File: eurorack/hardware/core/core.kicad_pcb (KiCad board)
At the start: 4 copper layers, 19.3 x 69.8 mm, 51 parts, among them J1 ConnNW, J2 ConnSW, J3 ConnNE, J4 ConnSE, J5 Power, J6 SWD, SW1 Reset, SW2 Boot0, U1 STM32F427VGT6, U2 TLV320AIC23BPW, U3 LM1117F-3.3, U4 LM4040C10IDBZR, Y1 Crystal

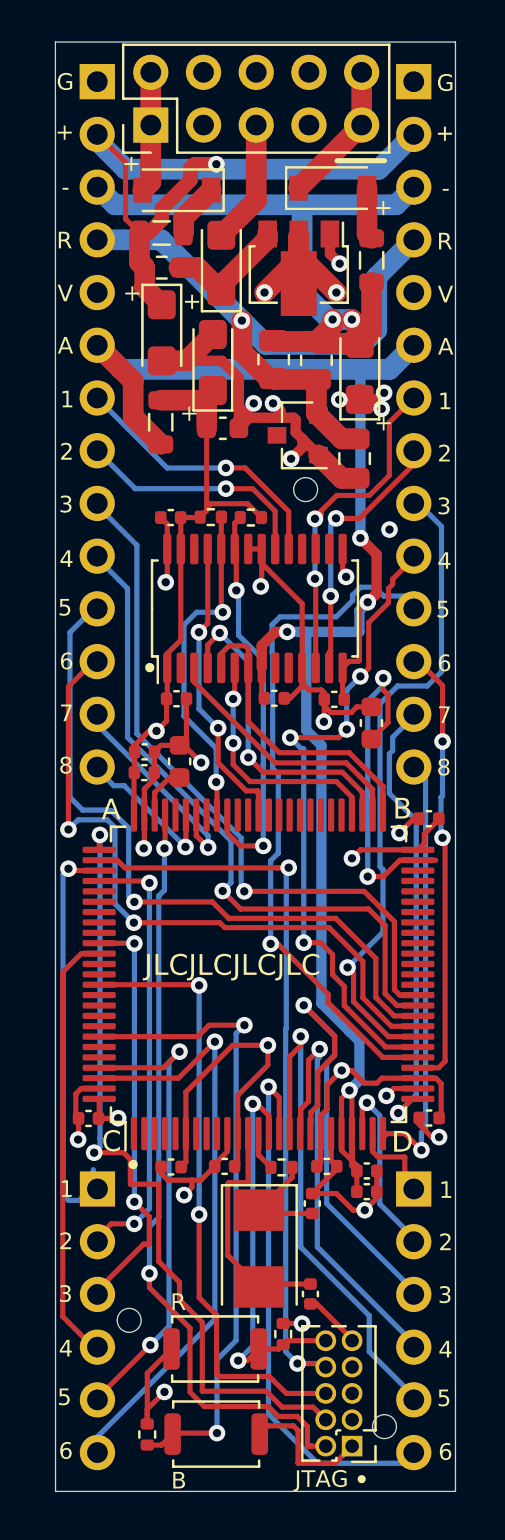
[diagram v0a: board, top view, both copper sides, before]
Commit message: Increase the height to 20 mm
Signed-off-by: Petr Horacek <hrck@protonmail.com>
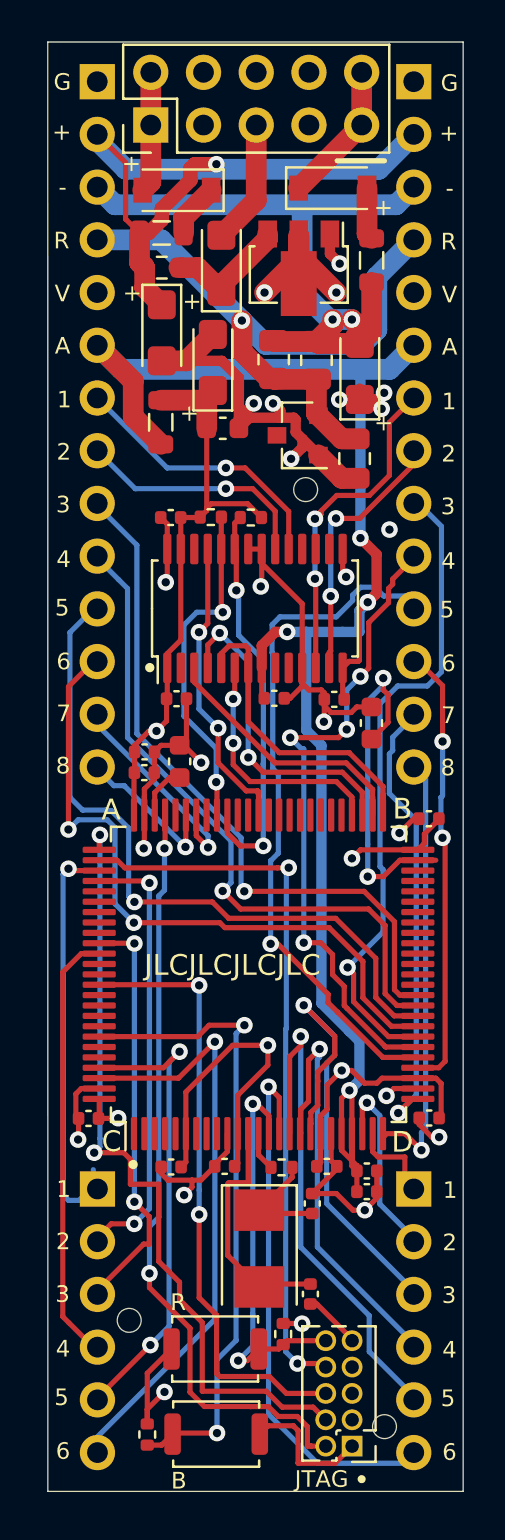
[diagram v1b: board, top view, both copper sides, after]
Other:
- board size 19.3 x 69.8 mm -> 20 x 69.8 mm
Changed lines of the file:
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@@
       (usegerberattributes true)
       (usegerberadvancedattributes true)
-      (creategerberjobfile true)
+      (creategerberjobfile false)
       (excludeedgelayer true)
       (linewidth 0.100000)
@@
   )
   (gr_line (start 154.314 70.75) (end 156.6 70.75) (layer F.SilkS) (width 0.25))
-  (gr_line (start 160.02 65.03) (end 140.75 65.03) (layer Edge.Cuts) (width 0.05))
-  (gr_line (start 160.02 134.86) (end 160.02 65.03) (layer Edge.Cuts) (width 0.05))
+  (gr_line (start 160.39 65.03) (end 140.375 65.03) (layer Edge.Cuts) (width 0.05))
+  (gr_line (start 160.39 134.86) (end 160.39 65.03) (layer Edge.Cuts) (width 0.05))
   (gr_circle (center 144.49 119.11) (end 144.604018 119.11) (layer F.SilkS) (width 0.22))
   (gr_circle (center 145.29 95.17) (end 145.404018 95.17) (layer F.SilkS) (width 0.22))
-  (gr_text - (at 159.55 72.08) (layer F.SilkS)
-    (effects (font (size 0.8 0.8) (thickness 0.15)))
-  )
-  (gr_text V (at 159.54 77.2) (layer F.SilkS)
-    (effects (font (size 0.8 0.8) (thickness 0.15)))
-  )
-  (gr_text + (at 159.51 69.42) (layer F.SilkS)
-    (effects (font (size 0.8 0.8) (thickness 0.15)))
-  )
-  (gr_text R (at 159.5 74.65) (layer F.SilkS)
-    (effects (font (size 0.8 0.8) (thickness 0.15)))
-  )
-  (gr_text G (at 159.54 67.01) (layer F.SilkS)
-    (effects (font (size 0.8 0.8) (thickness 0.15)))
-  )
-  (gr_text A (at 159.55 79.72) (layer F.SilkS)
-    (effects (font (size 0.8 0.8) (thickness 0.15)))
-  )
-  (gr_text 2 (at 141.26 122.82) (layer F.SilkS)
-    (effects (font (size 0.8 0.8) (thickness 0.15)))
-  )
-  (gr_text 1 (at 141.28 120.3) (layer F.SilkS)
-    (effects (font (size 0.8 0.8) (thickness 0.15)))
-  )
-  (gr_text 6 (at 141.25 132.92) (layer F.SilkS)
-    (effects (font (size 0.8 0.8) (thickness 0.15)))
-  )
-  (gr_text 3 (at 141.23 125.36) (layer F.SilkS)
-    (effects (font (size 0.8 0.8) (thickness 0.15)))
-  )
-  (gr_text 4 (at 141.25 127.99) (layer F.SilkS)
-    (effects (font (size 0.8 0.8) (thickness 0.15)))
-  )
-  (gr_text 5 (at 141.18 130.33) (layer F.SilkS)
-    (effects (font (size 0.8 0.8) (thickness 0.15)))
-  )
-  (gr_text 2 (at 159.55 122.87) (layer F.SilkS)
-    (effects (font (size 0.8 0.8) (thickness 0.15)))
-  )
-  (gr_text 1 (at 159.57 120.35) (layer F.SilkS)
-    (effects (font (size 0.8 0.8) (thickness 0.15)))
-  )
-  (gr_text 6 (at 159.54 132.97) (layer F.SilkS)
-    (effects (font (size 0.8 0.8) (thickness 0.15)))
-  )
-  (gr_text 3 (at 159.52 125.41) (layer F.SilkS)
-    (effects (font (size 0.8 0.8) (thickness 0.15)))
-  )
-  (gr_text 4 (at 159.54 128.04) (layer F.SilkS)
-    (effects (font (size 0.8 0.8) (thickness 0.15)))
-  )
-  (gr_text 5 (at 159.47 130.38) (layer F.SilkS)
-    (effects (font (size 0.8 0.8) (thickness 0.15)))
-  )
-  (gr_text 2 (at 159.5 84.87) (layer F.SilkS)
-    (effects (font (size 0.8 0.8) (thickness 0.15)))
-  )
-  (gr_text 1 (at 159.52 82.35) (layer F.SilkS)
-    (effects (font (size 0.8 0.8) (thickness 0.15)))
-  )
-  (gr_text 6 (at 159.49 94.97) (layer F.SilkS)
-    (effects (font (size 0.8 0.8) (thickness 0.15)))
-  )
-  (gr_text 3 (at 159.47 87.41) (layer F.SilkS)
-    (effects (font (size 0.8 0.8) (thickness 0.15)))
-  )
-  (gr_text 4 (at 159.49 90.04) (layer F.SilkS)
-    (effects (font (size 0.8 0.8) (thickness 0.15)))
-  )
-  (gr_text 5 (at 159.42 92.38) (layer F.SilkS)
-    (effects (font (size 0.8 0.8) (thickness 0.15)))
-  )
-  (gr_text 8 (at 159.46 99.99) (layer F.SilkS)
-    (effects (font (size 0.8 0.8) (thickness 0.15)))
-  )
-  (gr_text 7 (at 159.49 97.47) (layer F.SilkS)
+  (gr_text - (at 159.74 72.08) (layer F.SilkS)
+    (effects (font (size 0.8 0.8) (thickness 0.15)))
+  )
+  (gr_text V (at 159.73 77.2) (layer F.SilkS)
+    (effects (font (size 0.8 0.8) (thickness 0.15)))
+  )
+  (gr_text + (at 159.7 69.42) (layer F.SilkS)
+    (effects (font (size 0.8 0.8) (thickness 0.15)))
+  )
+  (gr_text R (at 159.69 74.65) (layer F.SilkS)
+    (effects (font (size 0.8 0.8) (thickness 0.15)))
+  )
+  (gr_text G (at 159.73 67.01) (layer F.SilkS)
+    (effects (font (size 0.8 0.8) (thickness 0.15)))
+  )
+  (gr_text A (at 159.74 79.72) (layer F.SilkS)
+    (effects (font (size 0.8 0.8) (thickness 0.15)))
+  )
+  (gr_text 2 (at 141.12 122.82) (layer F.SilkS)
+    (effects (font (size 0.8 0.8) (thickness 0.15)))
+  )
+  (gr_text 1 (at 141.14 120.3) (layer F.SilkS)
+    (effects (font (size 0.8 0.8) (thickness 0.15)))
+  )
+  (gr_text 6 (at 141.11 132.92) (layer F.SilkS)
+    (effects (font (size 0.8 0.8) (thickness 0.15)))
+  )
+  (gr_text 3 (at 141.09 125.36) (layer F.SilkS)
+    (effects (font (size 0.8 0.8) (thickness 0.15)))
+  )
+  (gr_text 4 (at 141.11 127.99) (layer F.SilkS)
+    (effects (font (size 0.8 0.8) (thickness 0.15)))
+  )
+  (gr_text 5 (at 141.04 130.33) (layer F.SilkS)
+    (effects (font (size 0.8 0.8) (thickness 0.15)))
+  )
+  (gr_text 2 (at 159.74 122.87) (layer F.SilkS)
+    (effects (font (size 0.8 0.8) (thickness 0.15)))
+  )
+  (gr_text 1 (at 159.76 120.35) (layer F.SilkS)
+    (effects (font (size 0.8 0.8) (thickness 0.15)))
+  )
+  (gr_text 6 (at 159.73 132.97) (layer F.SilkS)
+    (effects (font (size 0.8 0.8) (thickness 0.15)))
+  )
+  (gr_text 3 (at 159.71 125.41) (layer F.SilkS)
+    (effects (font (size 0.8 0.8) (thickness 0.15)))
+  )
+  (gr_text 4 (at 159.73 128.04) (layer F.SilkS)
+    (effects (font (size 0.8 0.8) (thickness 0.15)))
+  )
+  (gr_text 5 (at 159.66 130.38) (layer F.SilkS)
+    (effects (font (size 0.8 0.8) (thickness 0.15)))
+  )
+  (gr_text 2 (at 159.69 84.87) (layer F.SilkS)
+    (effects (font (size 0.8 0.8) (thickness 0.15)))
+  )
+  (gr_text 1 (at 159.71 82.35) (layer F.SilkS)
+    (effects (font (size 0.8 0.8) (thickness 0.15)))
+  )
+  (gr_text 6 (at 159.68 94.97) (layer F.SilkS)
+    (effects (font (size 0.8 0.8) (thickness 0.15)))
+  )
+  (gr_text 3 (at 159.66 87.41) (layer F.SilkS)
+    (effects (font (size 0.8 0.8) (thickness 0.15)))
+  )
+  (gr_text 4 (at 159.68 90.04) (layer F.SilkS)
+    (effects (font (size 0.8 0.8) (thickness 0.15)))
+  )
+  (gr_text 5 (at 159.61 92.38) (layer F.SilkS)
+    (effects (font (size 0.8 0.8) (thickness 0.15)))
+  )
+  (gr_text 8 (at 159.65 99.99) (layer F.SilkS)
+    (effects (font (size 0.8 0.8) (thickness 0.15)))
+  )
+  (gr_text 7 (at 159.68 97.47) (layer F.SilkS)
     (effects (font (size 0.8 0.8) (thickness 0.15)))
   )
@@
     (effects (font (size 1 1) (thickness 0.15)))
   )
-  (gr_text 8 (at 141.25 99.9) (layer F.SilkS)
-    (effects (font (size 0.8 0.8) (thickness 0.15)))
-  )
-  (gr_text 7 (at 141.28 97.38) (layer F.SilkS)
-    (effects (font (size 0.8 0.8) (thickness 0.15)))
-  )
-  (gr_text 6 (at 141.28 94.88) (layer F.SilkS)
-    (effects (font (size 0.8 0.8) (thickness 0.15)))
-  )
-  (gr_text 5 (at 141.21 92.29) (layer F.SilkS)
-    (effects (font (size 0.8 0.8) (thickness 0.15)))
-  )
-  (gr_text 4 (at 141.28 89.95) (layer F.SilkS)
-    (effects (font (size 0.8 0.8) (thickness 0.15)))
-  )
-  (gr_text 3 (at 141.26 87.32) (layer F.SilkS)
-    (effects (font (size 0.8 0.8) (thickness 0.15)))
-  )
-  (gr_text 1 (at 141.31 82.26) (layer F.SilkS)
-    (effects (font (size 0.8 0.8) (thickness 0.15)))
-  )
-  (gr_text 2 (at 141.29 84.78) (layer F.SilkS)
-    (effects (font (size 0.8 0.8) (thickness 0.15)))
-  )
-  (gr_text A (at 141.23 79.67) (layer F.SilkS)
-    (effects (font (size 0.8 0.8) (thickness 0.15)))
-  )
-  (gr_text V (at 141.22 77.15) (layer F.SilkS)
-    (effects (font (size 0.8 0.8) (thickness 0.15)))
-  )
-  (gr_text - (at 141.23 72.03) (layer F.SilkS)
-    (effects (font (size 0.8 0.8) (thickness 0.15)))
-  )
-  (gr_text R (at 141.18 74.6) (layer F.SilkS)
-    (effects (font (size 0.8 0.8) (thickness 0.15)))
-  )
-  (gr_text + (at 141.19 69.37) (layer F.SilkS)
-    (effects (font (size 0.8 0.8) (thickness 0.15)))
-  )
-  (gr_text G (at 141.22 66.96) (layer F.SilkS)
+  (gr_text 8 (at 141.11 99.9) (layer F.SilkS)
+    (effects (font (size 0.8 0.8) (thickness 0.15)))
+  )
+  (gr_text 7 (at 141.14 97.38) (layer F.SilkS)
+    (effects (font (size 0.8 0.8) (thickness 0.15)))
+  )
+  (gr_text 6 (at 141.14 94.88) (layer F.SilkS)
+    (effects (font (size 0.8 0.8) (thickness 0.15)))
+  )
+  (gr_text 5 (at 141.07 92.29) (layer F.SilkS)
+    (effects (font (size 0.8 0.8) (thickness 0.15)))
+  )
+  (gr_text 4 (at 141.14 89.95) (layer F.SilkS)
+    (effects (font (size 0.8 0.8) (thickness 0.15)))
+  )
+  (gr_text 3 (at 141.12 87.32) (layer F.SilkS)
+    (effects (font (size 0.8 0.8) (thickness 0.15)))
+  )
+  (gr_text 1 (at 141.17 82.26) (layer F.SilkS)
+    (effects (font (size 0.8 0.8) (thickness 0.15)))
+  )
+  (gr_text 2 (at 141.15 84.78) (layer F.SilkS)
+    (effects (font (size 0.8 0.8) (thickness 0.15)))
+  )
+  (gr_text A (at 141.09 79.67) (layer F.SilkS)
+    (effects (font (size 0.8 0.8) (thickness 0.15)))
+  )
+  (gr_text V (at 141.08 77.15) (layer F.SilkS)
+    (effects (font (size 0.8 0.8) (thickness 0.15)))
+  )
+  (gr_text - (at 141.09 72.03) (layer F.SilkS)
+    (effects (font (size 0.8 0.8) (thickness 0.15)))
+  )
+  (gr_text R (at 141.04 74.6) (layer F.SilkS)
+    (effects (font (size 0.8 0.8) (thickness 0.15)))
+  )
+  (gr_text + (at 141.05 69.37) (layer F.SilkS)
+    (effects (font (size 0.8 0.8) (thickness 0.15)))
+  )
+  (gr_text G (at 141.08 66.96) (layer F.SilkS)
     (effects (font (size 0.8 0.8) (thickness 0.15)))
   )
@@
     (effects (font (size 0.8 0.8) (thickness 0.15)))
   )
-  (gr_line (start 140.745 65.03) (end 140.75 134.86) (layer Edge.Cuts) (width 0.05))
-  (gr_line (start 140.75 134.86) (end 160.02 134.86) (layer Edge.Cuts) (width 0.05))
+  (gr_line (start 140.375 65.03) (end 140.38 134.86) (layer Edge.Cuts) (width 0.05))
+  (gr_line (start 140.38 134.86) (end 160.39 134.86) (layer Edge.Cuts) (width 0.05))
   (segment (start 152.15 119.730002) (end 150.570001 121.310001) (width 0.25) (layer F.Cu) (net 54) (status 20))
   (segment (start 152.15 119.25) (end 152.15 119.730002) (width 0.25) (layer F.Cu) (net 54) (status 10))

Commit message: Switch to STM32H743VIT6
It is twice the price of STM32F4 on JLCPCB and twice as fast.

Signed-off-by: Petr Horacek <hrck@protonmail.com>
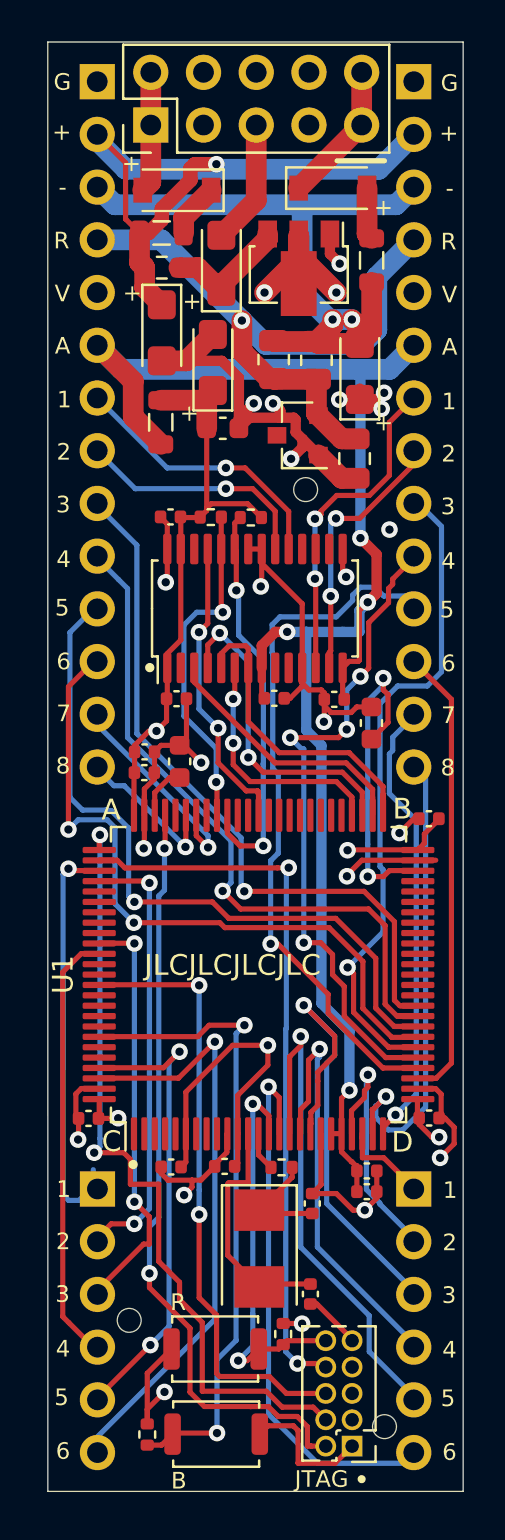
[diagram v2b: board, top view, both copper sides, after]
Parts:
- removed C19: 100n, Capacitor_SMD:C_0402_1005Metric
- U1: value STM32F427VGT6 -> STM32H743VIT6
- moved C15 32.2 mm to (146.3, 87.9), turned to 180 degrees
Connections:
- U1 pad 19: +3V3 -> GND
- U1 pad 20: GND -> +3.3VA
- U1 pad 22: +3.3VA -> PIN20
- U1 pad 23: PIN20 -> PIN19
- U1 pad 24: PIN19 -> PIN18
- U1 pad 25: PIN18 -> PIN17
- U1 pad 26: PIN17 -> GND
- U1 pad 27: GND -> +3V3
- U1 pad 28: +3V3 -> PIN16
- U1 pad 29: PIN16 -> PIN15
- U1 pad 30: PIN15 -> PIN14
- U1 pad 31: PIN14 -> PIN13
- U1 pad 32: PIN13 -> PIN4
- U1 pad 33: PIN4 -> PIN3
- U1 pad 34: PIN3 -> PIN2
- U1 pad 35: PIN2 -> PIN1
- U1 pad 36: PIN1 -> Net-(U1-Pad36)
- U1 pad 48: Net-(U1-Pad48) -> Net-(C3-Pad1)
- U1 pad 49: Net-(C3-Pad1) -> GND
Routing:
- net +3V3: track 77.7 -> 70.8 mm
- net +3.3VA: track 83.2 -> 78.6 mm
- net GND: track 189.4 -> 193.2 mm
- net PIN20: track 9.25 -> 12.2 mm
- net PIN18: track 21.1 -> 23.1 mm
- net PIN3: track 33.8 -> 35.4 mm
- net PIN2: track 32.7 -> 34.2 mm
- net PIN1: track 34.4 -> 35.8 mm
- net Net-(C3-Pad1): track 16.8 -> 15.8 mm
- net PIN19: track 4.29 -> 5.14 mm
- net PIN16: track 21.3 -> 22.0 mm, vias 2 -> 0
- net PIN4: track 33.0 -> 33.5 mm
- net PIN15: track 33.5 -> 34.1 mm
- net PIN14: track 31.6 -> 32.1 mm
- net PIN13: track 31.3 -> 31.8 mm
